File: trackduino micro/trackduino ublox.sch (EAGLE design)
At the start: 28 parts, among them IC1 74AHC1G125DBV, IC2 74AHC1G125DBV, IC3 74AHC1G125DBV, U1 ATMEGA168

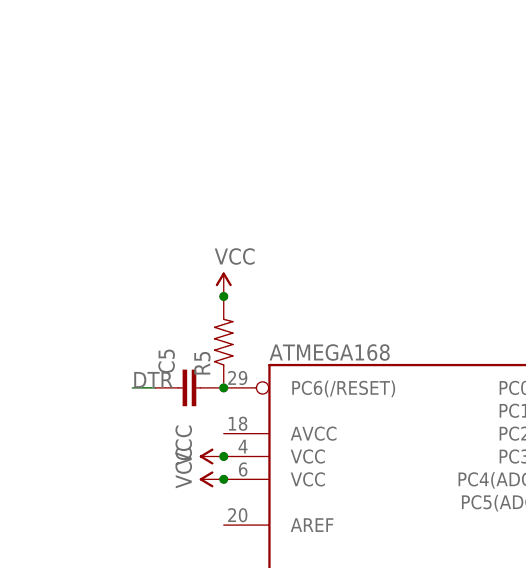
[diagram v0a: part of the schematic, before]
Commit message: reset switch
added a reset switch and improved RF ground fill.
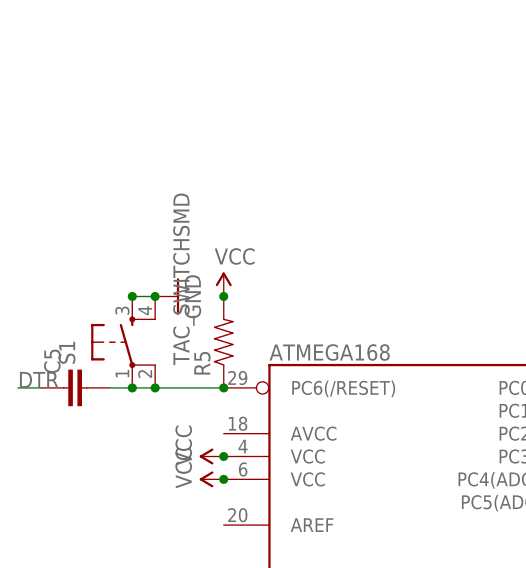
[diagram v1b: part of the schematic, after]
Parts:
- added S1: TAC_SWITCHSMD, SparkFun-Electromechanical:TAC_SWITCHSMD
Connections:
- net GND: now also S1.3, S1.4
- net N$9: now also S1.1, S1.2
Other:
- moved on the sheet: C5
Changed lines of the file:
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@@
 <part name="JP4" library="SparkFun-Connectors" deviceset="M02" device="PTH"/>
 <part name="JP5" library="SparkFun-Connectors" deviceset="M04" device="1X04_NO_SILK"/>
+<part name="S1" library="SparkFun-Electromechanical" deviceset="TAC_SWITCH" device="SMD" value="TAC_SWITCHSMD"/>
+<part name="GND23" library="SparkFun-Aesthetics" deviceset="GND" device=""/>
 </parts>
 <sheets>
@@
 <instance part="R5" gate="G$1" x="22.86" y="83.82" rot="R90"/>
 <instance part="SUPPLY10" gate="G$1" x="22.86" y="88.9"/>
-<instance part="C5" gate="G$1" x="20.32" y="78.74" rot="R90"/>
+<instance part="C5" gate="G$1" x="7.62" y="78.74" rot="R90"/>
 <instance part="JP3" gate="G$1" x="73.66" y="7.62" rot="R180"/>
 <instance part="JP4" gate="G$1" x="73.66" y="-5.08" rot="R180"/>
 <instance part="JP5" gate="G$1" x="17.78" y="-7.62"/>
+<instance part="S1" gate="S" x="12.7" y="83.82" rot="R90"/>
+<instance part="GND23" gate="1" x="17.78" y="88.9" rot="R90"/>
 </instances>
 <busses>
@@
 <junction x="149.86" y="10.16"/>
 </segment>
+<segment>
+<pinref part="S1" gate="S" pin="4"/>
+<pinref part="GND23" gate="1" pin="GND"/>
+<pinref part="S1" gate="S" pin="3"/>
+<wire x1="12.7" y1="88.9" x2="15.24" y2="88.9" width="0.1524" layer="91"/>
+<junction x="12.7" y="88.9"/>
+<junction x="15.24" y="88.9"/>
+</segment>
 </net>
 <net name="EN-5V" class="0">
@@
 <segment>
 <pinref part="C5" gate="G$1" pin="1"/>
-<wire x1="15.24" y1="78.74" x2="12.7" y2="78.74" width="0.1524" layer="91"/>
-<label x="12.7" y="78.74" size="1.778" layer="95"/>
+<wire x1="2.54" y1="78.74" x2="0" y2="78.74" width="0.1524" layer="91"/>
+<label x="0" y="78.74" size="1.778" layer="95"/>
 </segment>
 </net>
@@
 <pinref part="U1" gate="G$1" pin="PC6(/RESET)"/>
 <pinref part="R5" gate="G$1" pin="1"/>
+<pinref part="C5" gate="G$1" pin="2"/>
+<wire x1="10.16" y1="78.74" x2="12.7" y2="78.74" width="0.1524" layer="91"/>
 <junction x="22.86" y="78.74"/>
-<pinref part="C5" gate="G$1" pin="2"/>
-</segment>
-</net>
+<pinref part="S1" gate="S" pin="1"/>
+<wire x1="12.7" y1="78.74" x2="15.24" y2="78.74" width="0.1524" layer="91"/>
+<junction x="12.7" y="78.74"/>
+<pinref part="S1" gate="S" pin="2"/>
+<wire x1="15.24" y1="78.74" x2="22.86" y2="78.74" width="0.1524" layer="91"/>
+<junction x="15.24" y="78.74"/>
+</segment>
+</net>

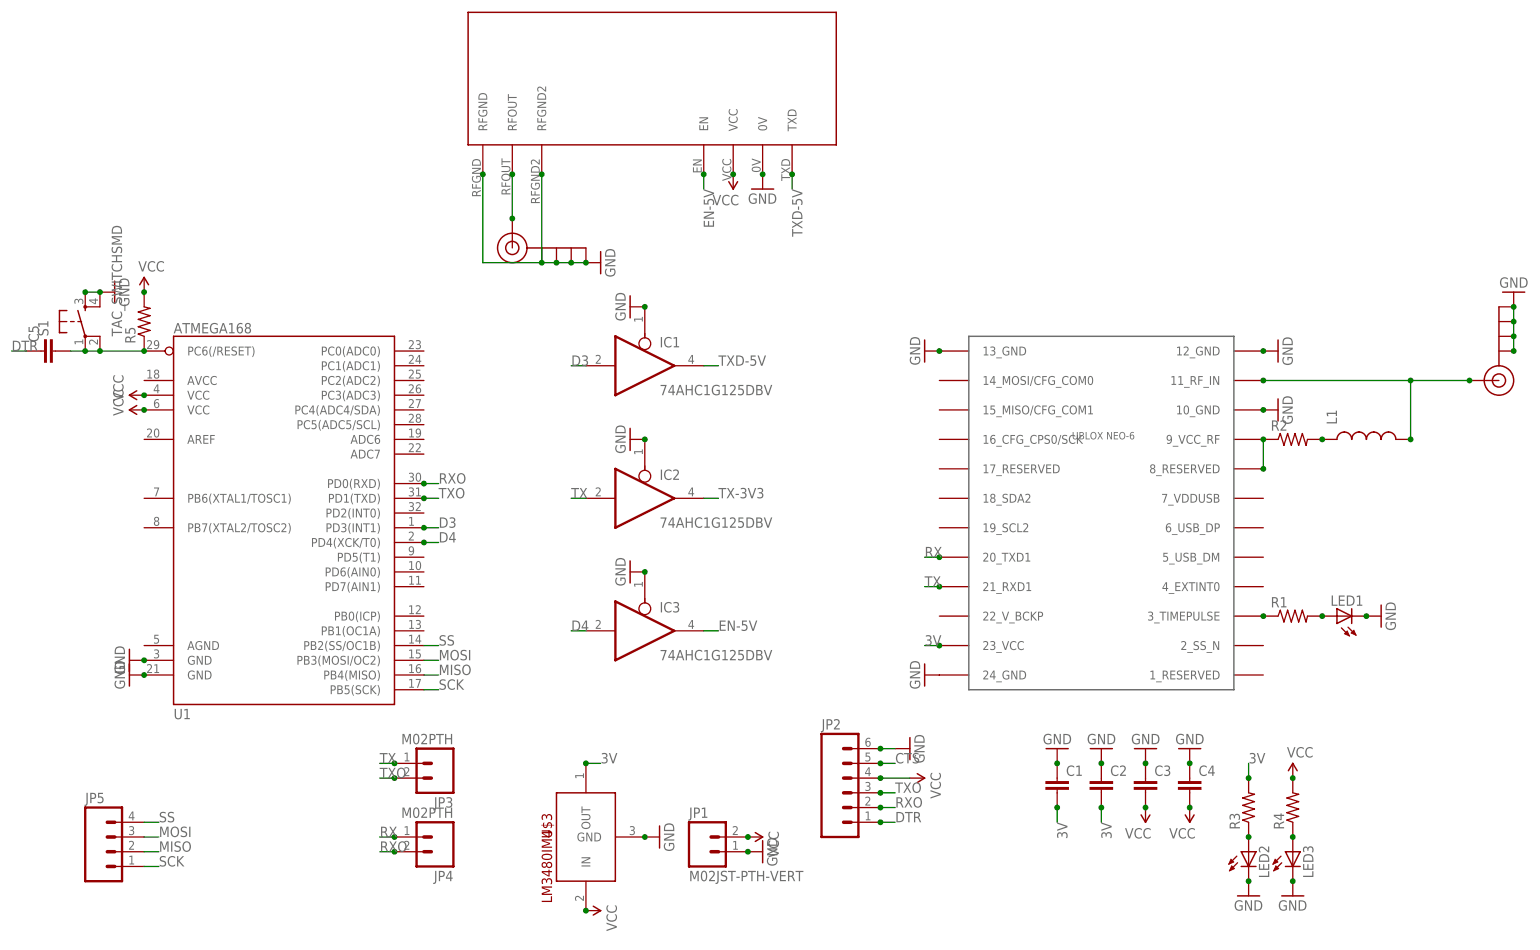
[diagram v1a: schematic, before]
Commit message: fixed missing vcc / ground connections
missed AVCC and AGND
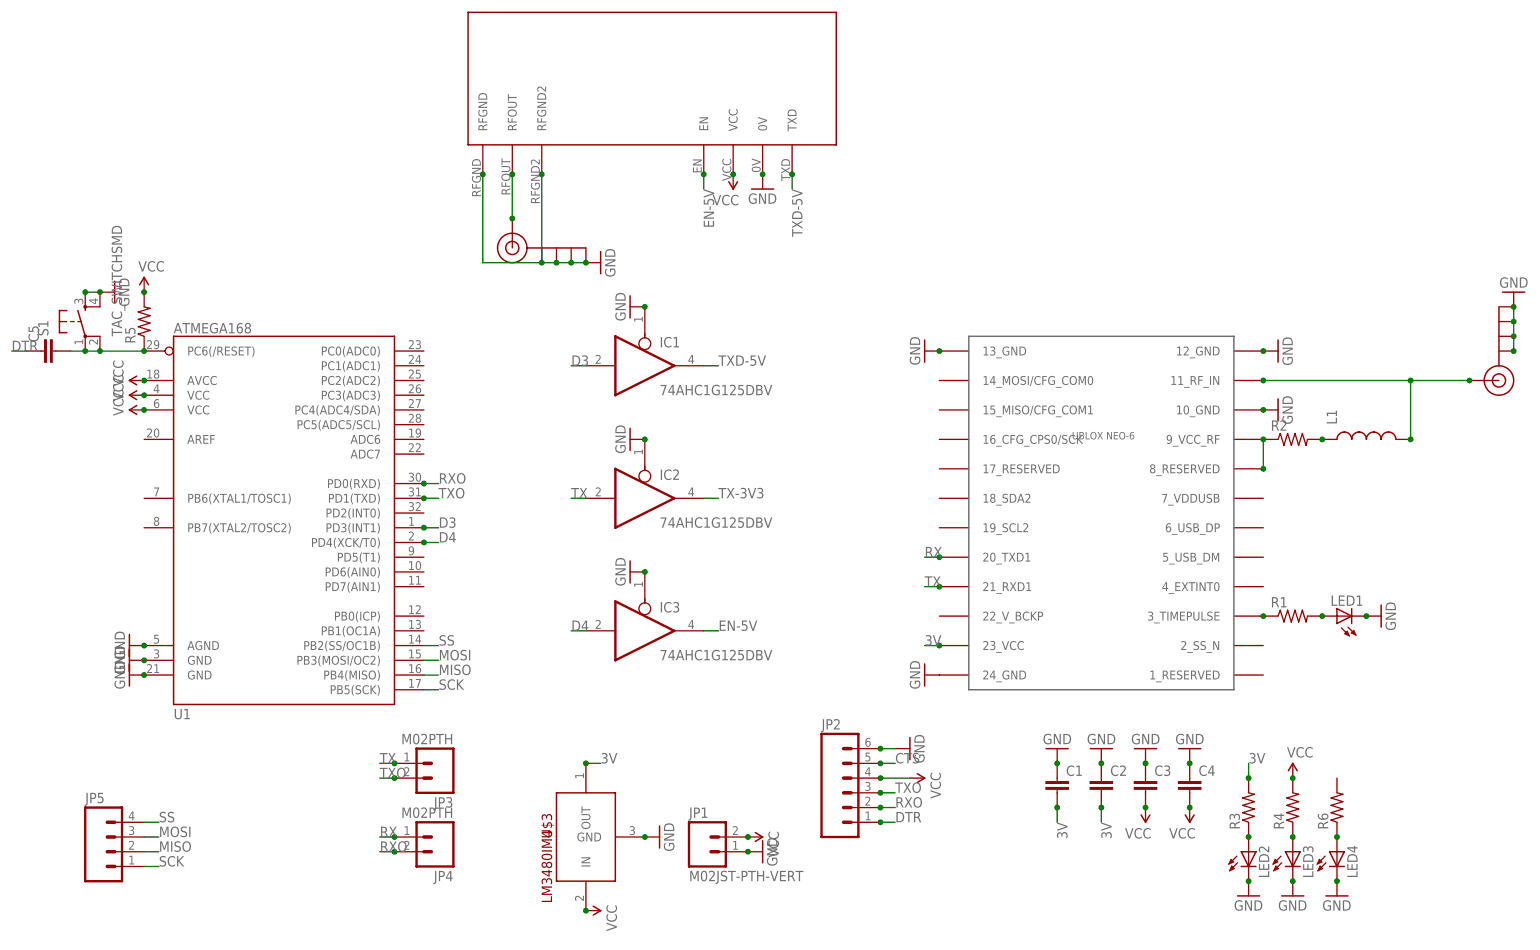
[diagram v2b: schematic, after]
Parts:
- added LED4: (no value), adafruit:LEDCHIP-LED0805
- added R6: (no value), SparkFun-Resistors:RESISTOR0805-RES
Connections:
- new net N$14: LED4.A, R6.1
- net GND: now also LED4.C, U1.AGND
- net VCC: now also U1.AVCC
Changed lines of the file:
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@@
 <part name="S1" library="SparkFun-Electromechanical" deviceset="TAC_SWITCH" device="SMD" value="TAC_SWITCHSMD"/>
 <part name="GND23" library="SparkFun-Aesthetics" deviceset="GND" device=""/>
+<part name="LED4" library="adafruit" deviceset="LED" device="CHIP-LED0805"/>
+<part name="R6" library="SparkFun-Resistors" deviceset="RESISTOR" device="0805-RES"/>
+<part name="GND24" library="SparkFun-Aesthetics" deviceset="GND" device=""/>
+<part name="SUPPLY11" library="SparkFun-Aesthetics" deviceset="VCC" device=""/>
+<part name="GND25" library="SparkFun-Aesthetics" deviceset="GND" device=""/>
 </parts>
 <sheets>
@@
 <instance part="S1" gate="S" x="12.7" y="83.82" rot="R90"/>
 <instance part="GND23" gate="1" x="17.78" y="88.9" rot="R90"/>
+<instance part="LED4" gate="G$1" x="228.6" y="-7.62"/>
+<instance part="R6" gate="G$1" x="228.6" y="0" rot="R90"/>
+<instance part="GND24" gate="1" x="228.6" y="-15.24"/>
+<instance part="SUPPLY11" gate="G$1" x="22.86" y="73.66" rot="R90"/>
+<instance part="GND25" gate="1" x="20.32" y="27.94" rot="R270"/>
 </instances>
 <busses>
@@
 <junction x="15.24" y="88.9"/>
 </segment>
+<segment>
+<pinref part="LED4" gate="G$1" pin="C"/>
+<pinref part="GND24" gate="1" pin="GND"/>
+<junction x="228.6" y="-12.7"/>
+</segment>
+<segment>
+<pinref part="U1" gate="G$1" pin="AGND"/>
+<pinref part="GND25" gate="1" pin="GND"/>
+<junction x="22.86" y="27.94"/>
+</segment>
 </net>
 <net name="EN-5V" class="0">
@@
 <pinref part="SUPPLY10" gate="G$1" pin="VCC"/>
 <junction x="22.86" y="88.9"/>
+</segment>
+<segment>
+<pinref part="U1" gate="G$1" pin="AVCC"/>
+<pinref part="SUPPLY11" gate="G$1" pin="VCC"/>
+<junction x="22.86" y="73.66"/>
 </segment>
 </net>
@@
 </segment>
 </net>
+<net name="N$14" class="0">
+<segment>
+<pinref part="LED4" gate="G$1" pin="A"/>
+<pinref part="R6" gate="G$1" pin="1"/>
+<junction x="228.6" y="-5.08"/>
+</segment>
+</net>

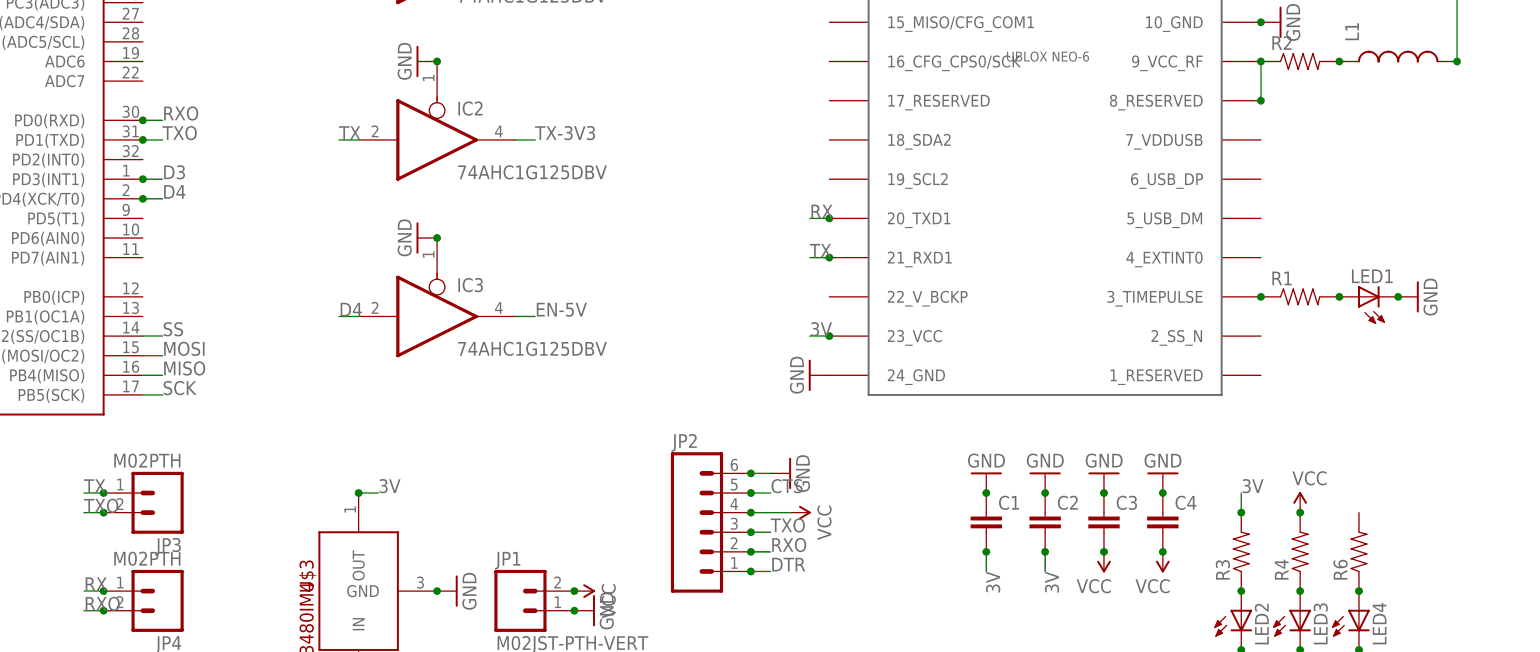
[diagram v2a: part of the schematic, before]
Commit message: added status LED
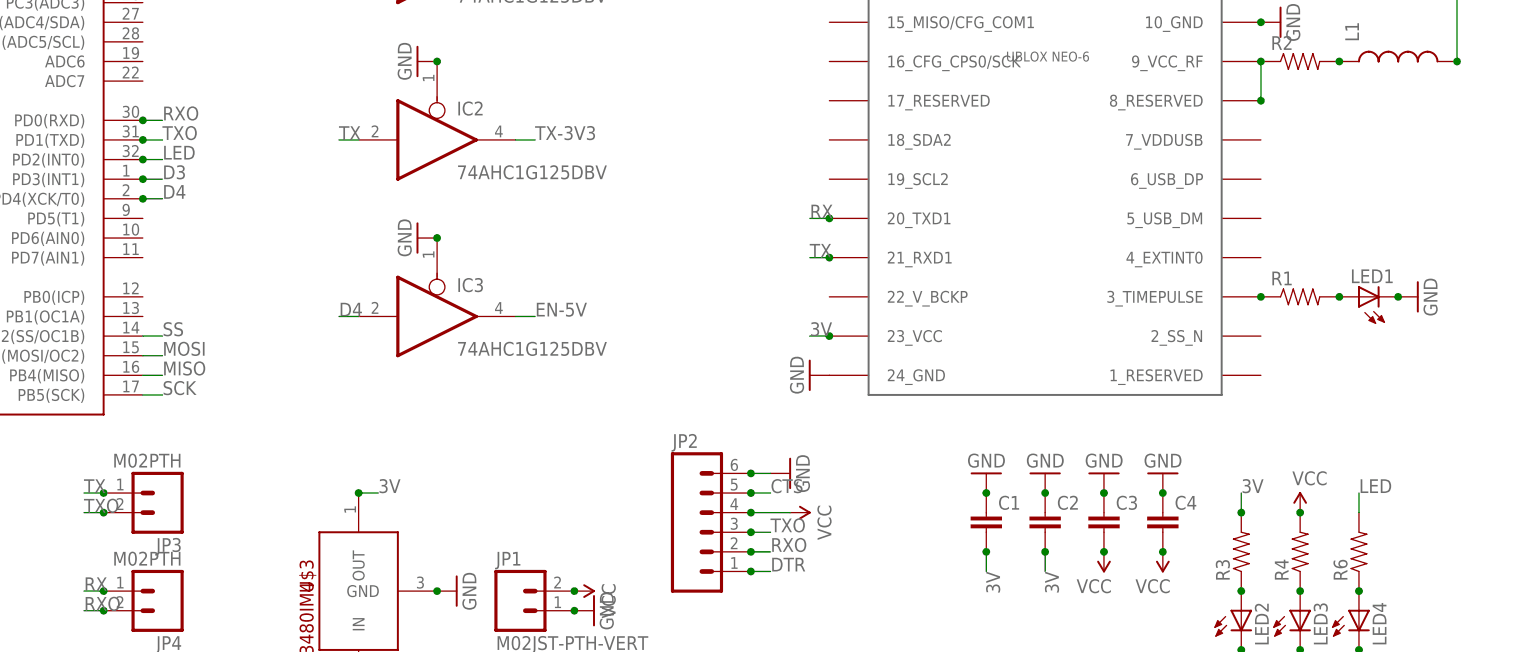
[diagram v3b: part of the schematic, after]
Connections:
- new net LED: R6.2, U1.PD2(INT0)
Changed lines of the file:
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@@
+</segment>
+</net>
+<net name="LED" class="0">
+<segment>
+<pinref part="U1" gate="G$1" pin="PD2(INT0)"/>
+<wire x1="71.12" y1="50.8" x2="73.66" y2="50.8" width="0.1524" layer="91"/>
+<label x="73.66" y="50.8" size="1.778" layer="95"/>
+<junction x="71.12" y="50.8"/>
+</segment>
+<segment>
+<pinref part="R6" gate="G$1" pin="2"/>
+<wire x1="228.6" y1="5.08" x2="228.6" y2="7.62" width="0.1524" layer="91"/>
+<label x="228.6" y="7.62" size="1.778" layer="95"/>
 </segment>
 </net>
